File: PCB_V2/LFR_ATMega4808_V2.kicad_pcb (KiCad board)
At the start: 2 copper layers, 70.5 x 90 mm, 74 parts, among them J1 Conn_02x02_Odd_Even, J10 Conn_01x03, J11 Conn_01x03, J2 Conn_02x05_Odd_Even, J5 Conn_01x03, J6 Conn_02x03_Odd_Even, J7 Conn_02x02_Odd_Even, J8 Conn_01x03, J9 Conn_01x03, Q1 PMOS_Si2333DDS, Q10 NMOS_BSR802NL6327HTSA1, Q11 NMOS_BSR802NL6327HTSA1, Q5 NMOS_BSR802NL6327HTSA1, Q6 NMOS_BSR802NL6327HTSA1, Q7 NMOS_BSR802NL6327HTSA1, Q8 NMOS_BSR802NL6327HTSA1, Q9 PMOS_Si2333DDS, U1 ATmega4808-A, U5 MCP1700x-330xxTO

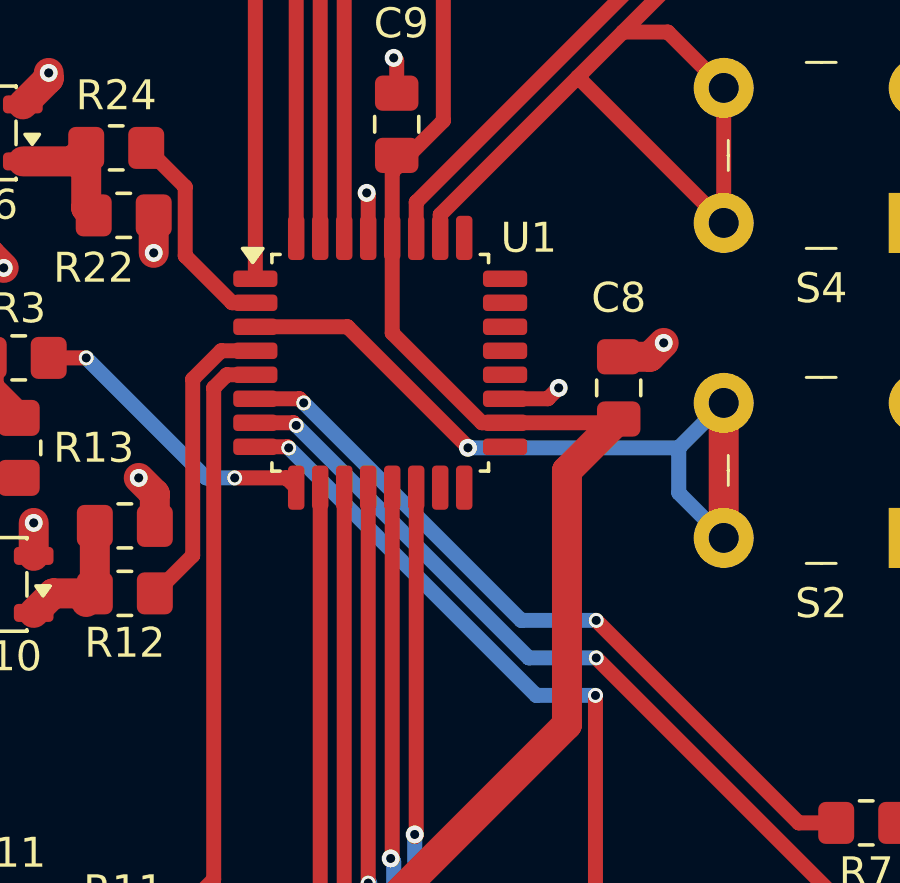
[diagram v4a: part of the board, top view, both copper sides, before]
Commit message: Redid the vias under the MCU
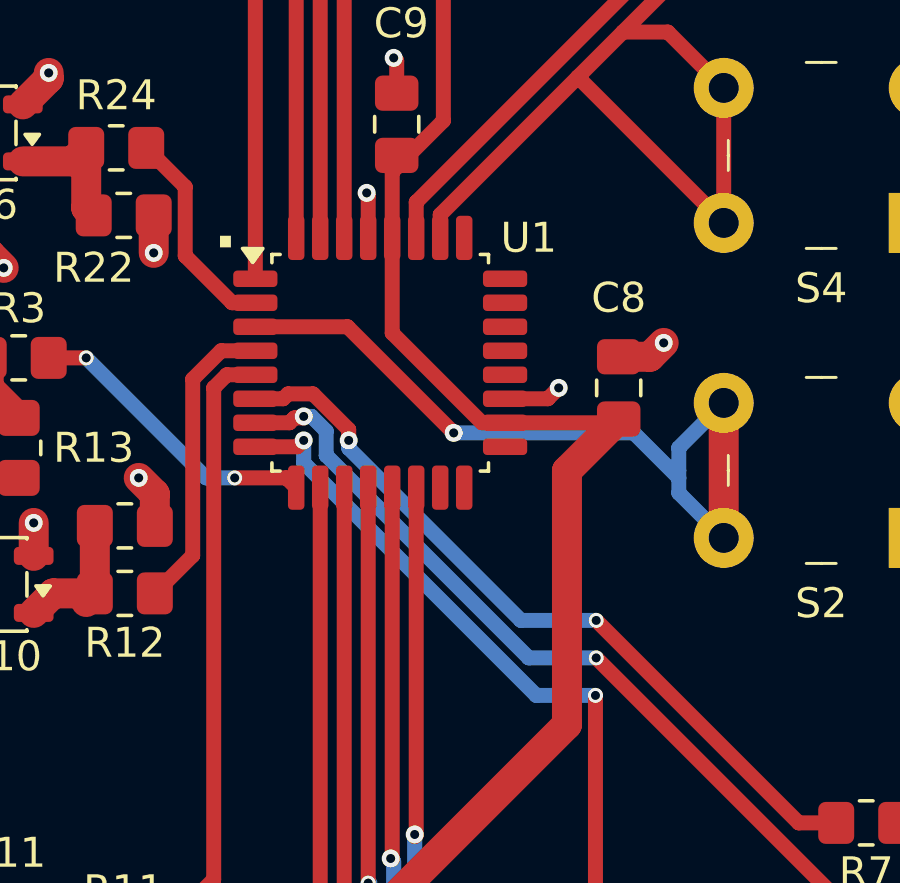
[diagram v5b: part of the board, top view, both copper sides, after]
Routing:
- net LED Green 1: track 29.9 -> 30.6 mm
- net LED Green 2: track 35.6 -> 36.2 mm
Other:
- board text added: "."
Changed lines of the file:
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@@
+		)
+	)
+	(gr_text "."
+		(at 146.5 107 0)
+		(layer "F.SilkS")
+		(effects
+			(font
+				(size 1.5 1.5)
+				(thickness 0.3)
+				(bold yes)
+			)
+			(justify left bottom)
 		)
 	)
@@
 	)
 	(segment
+		(start 147.8875 113.4625)
+		(end 149.2875 113.4625)
+		(width 0.5)
+		(layer "F.Cu")
+		(net "LED Green 2")
+	)
+	(segment
 		(start 167.25 138.55)
 		(end 167.25 139.25)
@@
 	)
 	(segment
-		(start 147.8875 113.4625)
-		(end 148.9625 113.4625)
+		(start 149.2875 113.4625)
+		(end 149.5 113.25)
 		(width 0.5)
 		(layer "F.Cu")
@@
 		(net "LED Green 2")
 	)
-	(segment
-		(start 148.9625 113.4625)
-		(end 149 113.5)
-		(width 0.5)
-		(layer "F.Cu")
-		(net "LED Green 2")
-	)
-	(via
-		(at 149 113.5)
-		(size 0.5)
-		(drill 0.3)
-		(layers "F.Cu" "B.Cu")
-		(net "LED Green 2")
-	)
 	(via
 		(at 159.225 121.75)
@@
 		(net "LED Green 2")
 	)
+	(via
+		(at 149.5 113.25)
+		(size 0.6)
+		(drill 0.3)
+		(layers "F.Cu" "B.Cu")
+		(net "LED Green 2")
+	)
+	(segment
+		(start 149.5 113.25)
+		(end 149.5 114)
+		(width 0.5)
+		(layer "B.Cu")
+		(net "LED Green 2")
+	)
 	(segment
 		(start 157.25 121.75)
@@
 	)
 	(segment
-		(start 149 113.5)
+		(start 149.5 114)
 		(end 157.25 121.75)
 		(width 0.5)
@@
 	)
 	(segment
+		(start 148.97741 111.699997)
+		(end 149.810661 111.699997)
+		(width 0.5)
+		(layer "F.Cu")
+		(net "LED Red")
+	)
+	(segment
+		(start 148.814907 111.8625)
+		(end 148.97741 111.699997)
+		(width 0.5)
+		(layer "F.Cu")
+		(net "LED Red")
+	)
+	(segment
+		(start 151 112.889336)
+		(end 151 113.25)
+		(width 0.5)
+		(layer "F.Cu")
+		(net "LED Red")
+	)
+	(segment
 		(start 159.25 119.25)
 		(end 166 126)
@@
 	)
 	(segment
-		(start 149.3625 111.8625)
-		(end 149.5 112)
-		(width 0.5)
-		(layer "F.Cu")
-		(net "LED Red")
-	)
-	(segment
 		(start 166 126)
 		(end 167.25 126)
@@
 	)
 	(segment
+		(start 149.810661 111.699997)
+		(end 151 112.889336)
+		(width 0.5)
+		(layer "F.Cu")
+		(net "LED Red")
+	)
+	(segment
 		(start 147.8875 111.8625)
-		(end 149.3625 111.8625)
+		(end 148.814907 111.8625)
 		(width 0.5)
 		(layer "F.Cu")
@@
 	)
 	(via
-		(at 149.5 112)
-		(size 0.5)
+		(at 151 113.25)
+		(size 0.6)
 		(drill 0.3)
 		(layers "F.Cu" "B.Cu")
@@
 	)
 	(segment
-		(start 149.5 112)
-		(end 156.75 119.25)
+		(start 156.73995 119.25)
+		(end 159.25 119.25)
 		(width 0.5)
 		(layer "B.Cu")
@@
 	)
 	(segment
-		(start 156.75 119.25)
-		(end 159.25 119.25)
+		(start 151 113.51005)
+		(end 156.73995 119.25)
 		(width 0.5)
 		(layer "B.Cu")
 		(net "LED Red")
+	)
+	(segment
+		(start 151 113.25)
+		(end 151 113.51005)
+		(width 0.5)
+		(layer "B.Cu")
+		(net "LED Red")
+	)
+	(segment
+		(start 147.8875 109.4625)
+		(end 150.9625 109.4625)
+		(width 0.5)
+		(layer "F.Cu")
+		(net "Button 1")
 	)
 	(segment
@@
 	(segment
 		(start 150.9625 109.4625)
-		(end 154.997299 113.497299)
+		(end 154.5 113)
 		(width 0.5)
 		(layer "F.Cu")
 		(net "Button 1")
 	)
-	(segment
-		(start 147.8875 109.4625)
-		(end 150.9625 109.4625)
-		(width 0.5)
-		(layer "F.Cu")
+	(via
+		(at 154.5 113)
+		(size 0.6)
+		(drill 0.3)
+		(layers "F.Cu" "B.Cu")
 		(net "Button 1")
 	)
 	(segment
-		(start 154.997299 113.497299)
-		(end 154.975 113.497299)
-		(width 0.5)
-		(layer "F.Cu")
+		(start 162.002701 114.5)
+		(end 162.002701 115.002701)
+		(width 0.5)
+		(layer "B.Cu")
 		(net "Button 1")
 	)
-	(via
-		(at 154.975 113.497299)
-		(size 0.6)
-		(drill 0.3)
-		(layers "F.Cu" "B.Cu")
+	(segment
+		(start 160.502701 113)
+		(end 162.002701 114.5)
+		(width 0.5)
+		(layer "B.Cu")
 		(net "Button 1")
 	)
 	(segment
-		(start 154.975 113.497299)
-		(end 162.002701 113.497299)
-		(width 0.5)
-		(layer "B.Cu")
-		(net "Button 1")
-	)
-	(segment
 		(start 162.002701 113.497299)
-		(end 162.002701 115.002701)
+		(end 162.002701 114.25)
 		(width 0.5)
 		(layer "B.Cu")
@@
 	)
 	(segment
+		(start 154.5 113)
+		(end 160.502701 113)
+		(width 0.5)
+		(layer "B.Cu")
+		(net "Button 1")
+	)
+	(segment
 		(start 162.002701 115.002701)
 		(end 163.5 116.5)
@@
 	)
 	(segment
-		(start 147.8875 112.6625)
-		(end 149.1625 112.6625)
+		(start 162.002701 114.25)
+		(end 162.002701 114.5)
+		(width 0.5)
+		(layer "B.Cu")
+		(net "Button 1")
+	)
+	(segment
+		(start 149.026839 112.6625)
+		(end 149.189339 112.5)
 		(width 0.5)
 		(layer "F.Cu")
@@
 	)
 	(segment
-		(start 149.1625 112.6625)
-		(end 149.25 112.75)
+		(start 149.5 112.5)
+		(end 149.5 112.449997)
 		(width 0.5)
 		(layer "F.Cu")
@@
 	)
 	(segment
+		(start 149.189339 112.5)
+		(end 149.5 112.5)
+		(width 0.5)
+		(layer "F.Cu")
+		(net "LED Green 1")
+	)
+	(segment
 		(start 159.25 120.5)
 		(end 167 128.25)
@@
 		(net "LED Green 1")
 	)
+	(segment
+		(start 147.8875 112.6625)
+		(end 149.026839 112.6625)
+		(width 0.5)
+		(layer "F.Cu")
+		(net "LED Green 1")
+	)
+	(via
+		(at 149.5 112.449997)
+		(size 0.6)
+		(drill 0.3)
+		(layers "F.Cu" "B.Cu")
+		(net "LED Green 1")
+	)
 	(via
 		(at 159.25 120.5)
@@
 		(net "LED Green 1")
 	)
-	(via
-		(at 149.25 112.75)
-		(size 0.5)
-		(drill 0.3)
-		(layers "F.Cu" "B.Cu")
+	(segment
+		(start 150.25 113.75)
+		(end 157 120.5)
+		(width 0.5)
+		(layer "B.Cu")
 		(net "LED Green 1")
 	)
 	(segment
-		(start 149.25 112.75)
-		(end 157 120.5)
+		(start 149.5 112.449997)
+		(end 149.760658 112.449997)
 		(width 0.5)
 		(layer "B.Cu")
@@
 		(width 0.5)
 		(layer "B.Cu")
+		(net "LED Green 1")
+	)
+	(segment
+		(start 150.25 112.939339)
+		(end 150.25 113.75)
+		(width 0.5)
+		(layer "B.Cu")
+		(net "LED Green 1")
+	)
+	(segment
+		(start 149.760658 112.449997)
+		(end 150.25 112.939339)
+		(width 0.5)
+		(layer "B.Cu")
